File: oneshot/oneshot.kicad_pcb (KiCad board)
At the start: 4 copper layers, 313.1 x 185.6 mm, 160 parts, among them J1 AudioJack2, J10 AudioJack2, J11 Conn_02x05_Odd_Even, J16 Conn_01x02 (3u), J18 AudioJack2, J2 Conn_01x04, J20 AudioJack2, J25 Conn_01x04, J26 Conn_01x04, J27 Conn_01x04, J29 AudioJack2, J3 Conn_01x04, J31 AudioJack2, J33 AudioJack2, J34 AudioJack2, J35 AudioJack2, J36 AudioJack2, J37 AudioJack2, J38 AudioJack2, J39 AudioJack2, J4 Conn_01x04, J40 AudioJack2, J5 AudioJack2, J6 Conn_01x04, J7 Conn_01x04, J8 Conn_01x04, J9 AudioJack2, Q1 MMBT3904, U1 TL072, U2 TL072, U3 ONESHOT, U4 TL072, U5 LM1117DT-5.0, U6 LM358, U7 LM358, U8 LM358, U9 LM358

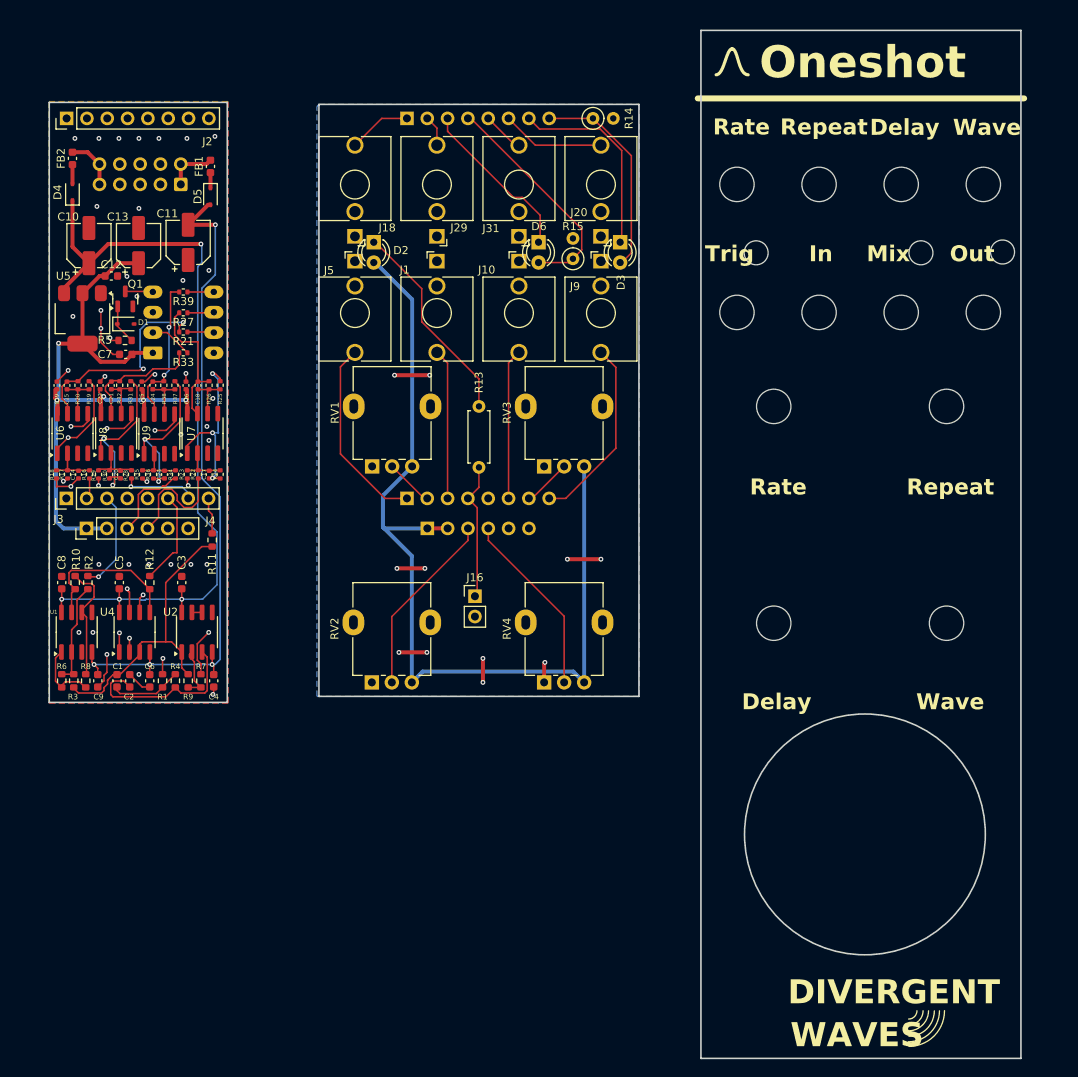
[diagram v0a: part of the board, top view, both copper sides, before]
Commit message: Updating oneshot project files
These are for the 1.1 (Prototype 2) PCBs
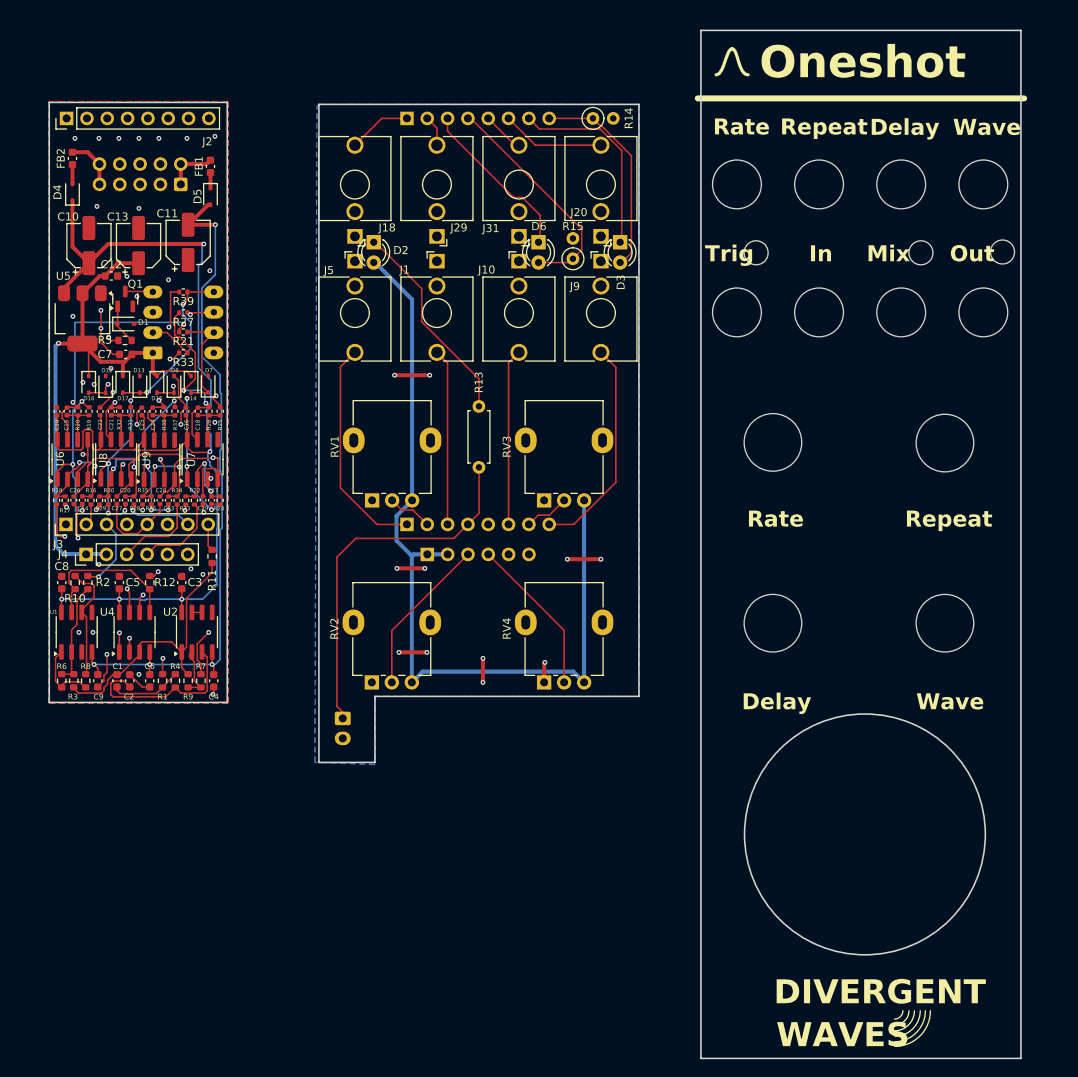
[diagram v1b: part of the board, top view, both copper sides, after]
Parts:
- added C26: 100n, Capacitor_SMD:C_0402_1005Metric, F.Cu at (167.1, 142.2)
- added C27: 100n, Capacitor_SMD:C_0402_1005Metric, F.Cu at (172.5, 142.2)
- added C28: 100n, Capacitor_SMD:C_0402_1005Metric, F.Cu at (177.9, 142.2)
- added C29: 100n, Capacitor_SMD:C_0402_1005Metric, F.Cu at (183.3, 142.2)
- added D12: BAT42, Diode_SMD:D_SOD-323, F.Cu at (171.1, 127.8)
- added D13: BAT42, Diode_SMD:D_SOD-323, F.Cu at (175.4, 127.8)
- added D14: BAT42, Diode_SMD:D_SOD-323, F.Cu at (181.8, 127.8)
- added D15: BAT42, Diode_SMD:D_SOD-323, F.Cu at (177.5, 127.8)
- added D16: BAT42, Diode_SMD:D_SOD-323, F.Cu at (169.0, 127.8)
- added D17: BAT42, Diode_SMD:D_SOD-323, F.Cu at (173.2, 127.8)
- added D7: BAT42, Diode_SMD:D_SOD-323, F.Cu at (183.9, 127.7)
- added D8: BAT42, Diode_SMD:D_SOD-323, F.Cu at (179.6, 127.8)
- J16: footprint Connector_PinHeader_2.54mm:PinHeader_1x02_P2.54mm_Vertical -> Connector_JST:JST_XH_B2B-XH-A_1x02_P2.50mm_Vertical; moved to B.Cu
- moved J16 22.5 mm to (200.7, 169.5), turned to -90 degrees
- moved H15 4.59 mm to (276.0, 135.1)
- moved H16 4.50 mm to (254.5, 135.0)
- moved RV1 4.25 mm to (204.4, 142.2)
- moved RV3 4.25 mm to (225.9, 142.2)
- moved R22 3.29 mm to (182.2, 142.2)
- moved C20 3.27 mm to (173.6, 142.2)
- moved R28 3.26 mm to (174.6, 142.2)
- moved R17 3.26 mm to (166.0, 142.2)
- moved R36 3.26 mm to (176.8, 142.2)
- moved R23 3.26 mm to (181.1, 142.2)
- moved R34 3.26 mm to (180.0, 142.2)
- moved R16 3.25 mm to (169.2, 142.2)
- moved R30 3.25 mm to (171.4, 142.2)
- moved R29 3.25 mm to (170.3, 142.2)
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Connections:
- C16 pad 1: +5V -> +12V
- C19 pad 1: +5V -> +12V
- C22 pad 1: +5V -> +12V
- C25 pad 1: +5V -> +12V
- U6 pad 4: Earth -> -12V
- U6 pad 8: +5V -> +12V
- U7 pad 4: Earth -> -12V
- U7 pad 8: +5V -> +12V
- U8 pad 4: Earth -> -12V
- U8 pad 8: +5V -> +12V
- U9 pad 4: Earth -> -12V
- U9 pad 8: +5V -> +12V
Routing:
- net -12V: track 88.1 -> 133.5 mm, vias 4 -> 5
- net +12V: track 101.9 -> 145.2 mm, vias 4 -> 5
- net /TRIGGER_INVERTED_TOP: track 17.3 -> 46.2 mm
- net +5V: track 308.7 -> 285.9 mm, vias 5 -> 1
- net Earth: track 115.3 -> 136.6 mm, vias 64 -> 62
- net DELAY: track 3.30 -> 21.8 mm, vias 0 -> 2
- net WAVEFORM: track 3.33 -> 16.7 mm, vias 0 -> 2
- net REPEATS: track 5.37 -> 17.7 mm, vias 0 -> 1
- net RATE: track 3.33 -> 13.9 mm
- net Net-(U8A--): track 6.24 -> 14.4 mm, vias 0 -> 2
- net /TRIGGER_INVERTED: track 31.0 -> 39.0 mm
- net Net-(C14-Pad2): track 22.5 -> 30.1 mm, vias 2 -> 4
- net Net-(U6A--): track 6.25 -> 13.8 mm, vias 0 -> 2
- net /MIX_LED_OUT_BOT: track 68.2 -> 75.6 mm
- net /TRIG_IN_BOT: track 23.9 -> 31.3 mm
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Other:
- outline, holes or cut-outs redrawn
- board text added: "Long"
- board text added: "Oneshot 1.1 (Prototype 2) Tom Carlson 2025 hello@divergentwaves.co.uk"
- board text added: "Short"
